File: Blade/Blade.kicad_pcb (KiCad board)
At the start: 2 copper layers, 120 x 40 mm, 43 parts, among them J1 USB_C_Receptacle_USB2.0, J2 THD-02-R, J3 Micro_SD_Card_Det, J4 Conn_01x03, J5 JST_SHBM04B-SRSS-TB, J6 Conn_02x07_Odd_Even, J7 Conn_01x22_Female, J8 Bus_M.2_Socket_M, SW1 Right angle Tact button, U1 TPD4EUSB30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

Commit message: Minor corrections to Blade Design
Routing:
- net /+5v: track 166.6 -> 165.2 mm
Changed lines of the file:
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@@
 			)
 		)
+		(model "${KIPRJMOD}/CM5IO.3dshapes/CM5R5-3dstep.step"
+			(hide yes)
+			(offset
+				(xyz 36.5 -3.5 1)
+			)
+			(scale
+				(xyz 1 1 1)
+			)
+			(rotate
+				(xyz 0 0 -90)
+			)
+		)
 	)
 	(footprint "Package_SON:USON-10_2.5x1.0mm_P0.5mm"
@@
 	)
 	(via
-		(at 109.41 63.81)
+		(at 111.94 63.95)
 		(size 0.3)
 		(drill 0.2)
@@
 	)
 	(via
-		(at 110.71 64.9)
+		(at 113.76 63.61)
 		(size 0.3)
 		(drill 0.2)
@@
 	)
 	(via
-		(at 114.3 64.92)
+		(at 114.4 61.09)
 		(size 0.3)
 		(drill 0.2)
@@
 	)
 	(segment
-		(start 109.25 60)
-		(end 109.41 60.16)
+		(start 110.71 61.46)
+		(end 109.25 60)
 		(width 0.2)
 		(layer "B.Cu")
@@
 	)
 	(segment
-		(start 109.25 60)
-		(end 110.71 61.46)
+		(start 109.41 60.16)
+		(end 109.25 60)
 		(width 0.2)
 		(layer "B.Cu")
@@
 	)
 	(segment
-		(start 114.17 64.92)
-		(end 114.3 64.92)
-		(width 0.2)
-		(layer "B.Cu")
-		(net 1)
-	)
-	(segment
 		(start 140.76 68.75)
 		(end 140.66 68.85)
@@
 	)
 	(segment
+		(start 111.61 61.46)
+		(end 110.71 61.46)
+		(width 0.2)
+		(layer "B.Cu")
+		(net 1)
+	)
+	(segment
 		(start 142 70.35)
 		(end 140.66 69.01)
@@
 	)
 	(segment
+		(start 113.76 63.61)
+		(end 111.61 61.46)
+		(width 0.2)
+		(layer "B.Cu")
+		(net 1)
+	)
+	(segment
 		(start 142.775 50.75)
 		(end 141.56 50.75)
@@
 	)
 	(segment
+		(start 114.4 61.09)
+		(end 110.34 61.09)
+		(width 0.2)
+		(layer "B.Cu")
+		(net 1)
+	)
+	(segment
 		(start 64.56 62.7)
 		(end 65.93 61.33)
@@
 	)
 	(segment
-		(start 144.125 58.25)
-		(end 144.125 58.275)
+		(start 109.41 61.42)
+		(end 109.41 60.16)
 		(width 0.2)
 		(layer "B.Cu")
@@
 	)
 	(segment
-		(start 109.41 60.16)
-		(end 109.41 63.81)
+		(start 144.125 58.25)
+		(end 144.125 58.275)
 		(width 0.2)
 		(layer "B.Cu")
@@
 	)
 	(segment
-		(start 109.25 60)
-		(end 114.17 64.92)
-		(width 0.2)
-		(layer "B.Cu")
-		(net 1)
-	)
-	(segment
 		(start 141.48 63.78)
 		(end 141.48 63.58)
@@
 	)
 	(segment
-		(start 110.71 61.46)
-		(end 110.71 64.9)
+		(start 110.34 61.09)
+		(end 109.25 60)
+		(width 0.2)
+		(layer "B.Cu")
+		(net 1)
+	)
+	(segment
+		(start 111.94 63.95)
+		(end 109.41 61.42)
 		(width 0.2)
 		(layer "B.Cu")
@@
 	)
 	(segment
+		(start 109.12 65.06)
+		(end 102.62 58.56)
+		(width 0.5)
+		(layer "B.Cu")
+		(net 2)
+	)
+	(segment
 		(start 161.1 57.175)
 		(end 162.05 58.125)
@@
 	)
 	(segment
-		(start 113.417107 66.48647)
-		(end 110.54647 66.48647)
-		(width 0.5)
-		(layer "B.Cu")
-		(net 2)
-	)
-	(segment
 		(start 162.05 59.475)
 		(end 160.825 60.7)
@@
 	)
 	(segment
-		(start 119.721905 73.08)
-		(end 117.23 73.08)
+		(start 160.125 63.71)
+		(end 160.125 66.015)
 		(width 0.5)
 		(layer "B.Cu")
@@
 	)
 	(segment
-		(start 160.125 63.71)
-		(end 160.125 66.015)
+		(start 111.990637 65.06)
+		(end 109.12 65.06)
 		(width 0.5)
 		(layer "B.Cu")
@@
 	)
 	(segment
-		(start 117.23 70.299363)
-		(end 113.417107 66.48647)
-		(width 0.5)
-		(layer "B.Cu")
-		(net 2)
-	)
-	(segment
 		(start 159.72 76.58)
 		(end 159.72 66.42)
@@
 	)
 	(segment
-		(start 117.23 73.08)
-		(end 117.23 70.299363)
+		(start 122.35 77.39)
+		(end 122.35 75.419363)
 		(width 0.5)
 		(layer "B.Cu")
@@
 	)
 	(segment
-		(start 122.35 75.708095)
-		(end 119.721905 73.08)
-		(width 0.5)
-		(layer "B.Cu")
-		(net 2)
-	)
-	(segment
-		(start 122.35 77.39)
-		(end 122.35 75.708095)
-		(width 0.5)
-		(layer "B.Cu")
-		(net 2)
-	)
-	(segment
-		(start 110.54647 66.48647)
-		(end 102.62 58.56)
+		(start 122.35 75.419363)
+		(end 111.990637 65.06)
 		(width 0.5)
 		(layer "B.Cu")
@@
 		(start 106.96 46.01)
 		(end 105.7875 46.01)
-		(width 0.2)
+		(width 0.5)
 		(layer "B.Cu")
 		(net 7)
@@
 	)
 	(segment
-		(start 102.14 46.01)
-		(end 102.1375 46.0125)
-		(width 0.2)
-		(layer "B.Cu")
-		(net 8)
-	)
-	(segment
 		(start 55.65 73)
 		(end 57.315 74.665)
@@
 	)
 	(segment
+		(start 102.14 46.01)
+		(end 102.1375 46.0125)
+		(width 0.5)
+		(layer "B.Cu")
+		(net 8)
+	)
+	(segment
 		(start 153.565 70.04)
 		(end 153.565 71.04)
@@
 	)
 	(segment
-		(start 104.2125 46.01)
-		(end 102.14 46.01)
-		(width 0.2)
+		(start 57.315 63.945)
+		(end 55.65 65.61)
+		(width 0.5)
 		(layer "B.Cu")
 		(net 8)
 	)
 	(segment
-		(start 57.315 63.945)
-		(end 55.65 65.61)
+		(start 104.2125 46.01)
+		(end 102.14 46.01)
 		(width 0.5)
 		(layer "B.Cu")
@@
 	)
 	(segment
-		(start 108.96 46.01)
-		(end 107.98 46.01)
+		(start 110.85 52.467158)
+		(end 114.157841 55.774999)
 		(width 0.1)
 		(layer "B.Cu")
@@
 	)
 	(segment
-		(start 110.85 52.467158)
-		(end 114.157841 55.774999)
-		(width 0.1)
+		(start 107.98 46.01)
+		(end 108.96 46.01)
+		(width 0.2)
 		(layer "B.Cu")
 		(net 146)
@@
 	)
 	(group ""
-		(members "0492ae78-a7de-4e5f-a749-5bdb550cd74f" "7da5246a-e259-4a54-8e14-de82bd062404"
-			"979045ba-a9a8-4425-887a-53068e6b7b0f"
-		)
+		(members "7da5246a-e259-4a54-8e14-de82bd062404" "979045ba-a9a8-4425-887a-53068e6b7b0f")
 	)
 	(generated

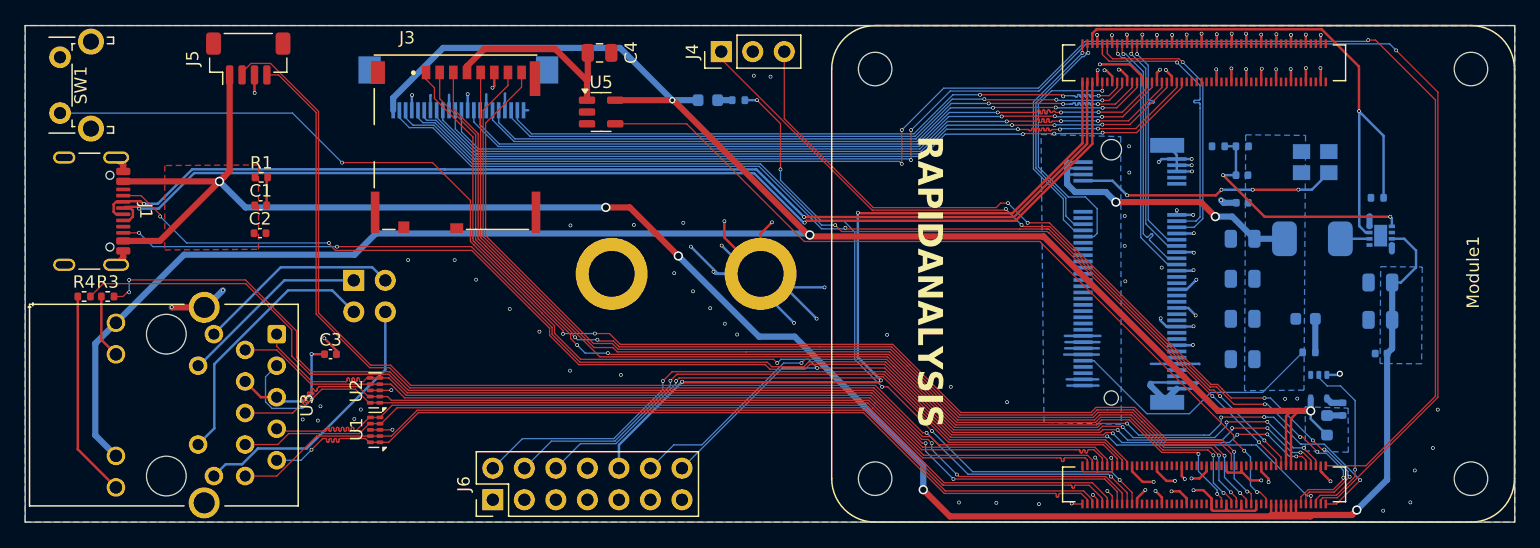
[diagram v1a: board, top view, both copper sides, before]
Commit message: Sent for production to PCBWay.
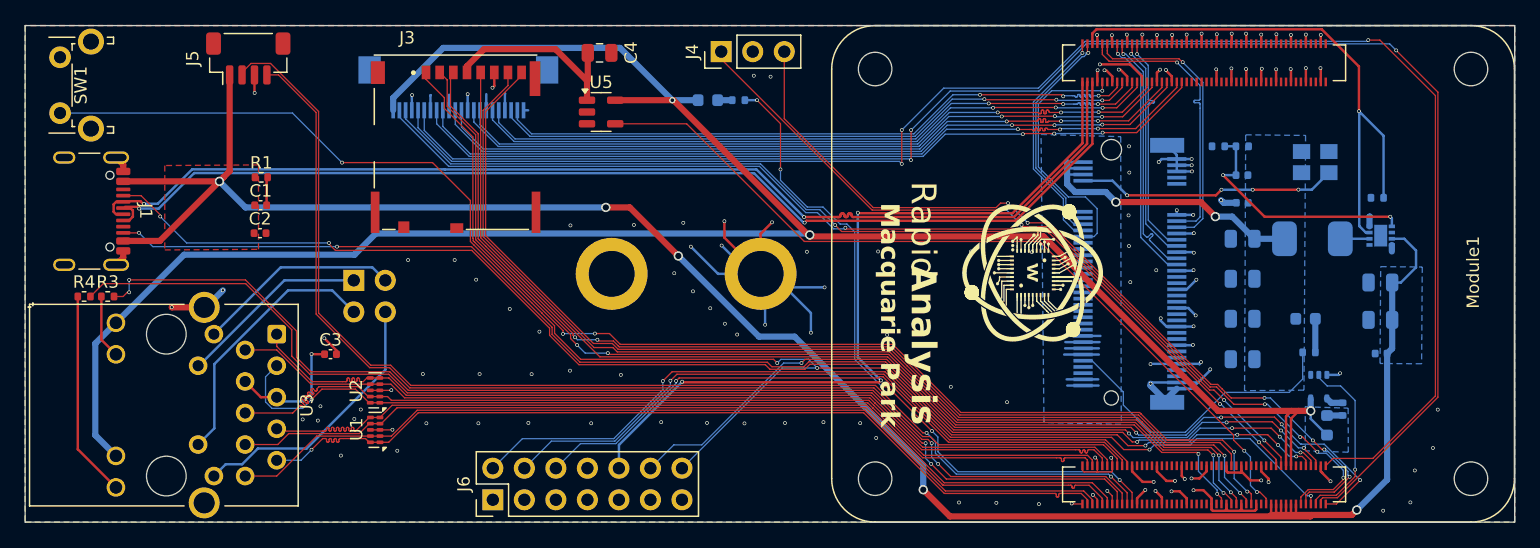
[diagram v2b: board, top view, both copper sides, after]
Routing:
- net Net-(J8-DAS/~{DSS}/~{LED1}): track 21.5 -> 24.6 mm
- net GND: track 171.6 -> 169.7 mm, vias 120 -> 141
- net /USB2_N: track 90.1 -> 90.8 mm
- net /CM5_HighSpeed/DPHY0_D2_N: track 62.6 -> 61.9 mm
- net Net-(Module1A-LED_nACT): track 53.9 -> 54.6 mm
- net /CM5_GPIO ( Ethernet, GPIO, SDCARD)/nRPIBOOT: track 74.4 -> 75.1 mm
- net /CM5_GPIO ( Ethernet, GPIO, SDCARD)/CAM_GPIO1: track 126.8 -> 127.5 mm
- net /CM5_GPIO ( Ethernet, GPIO, SDCARD)/CAM_GPIO0: track 128.4 -> 129.0 mm
- net /CM5_GPIO ( Ethernet, GPIO, SDCARD)/PWM: track 96.5 -> 97.1 mm
- net /CM5_GPIO ( Ethernet, GPIO, SDCARD)/PMIC_ENABLE: track 70.2 -> 69.7 mm
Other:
- board text added: "Analysis"
- board text added: "Macquarie Park"
- board text added: "Rapid"
- board text removed: "RAPIDANALYSIS"
